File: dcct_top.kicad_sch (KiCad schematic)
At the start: 0 parts

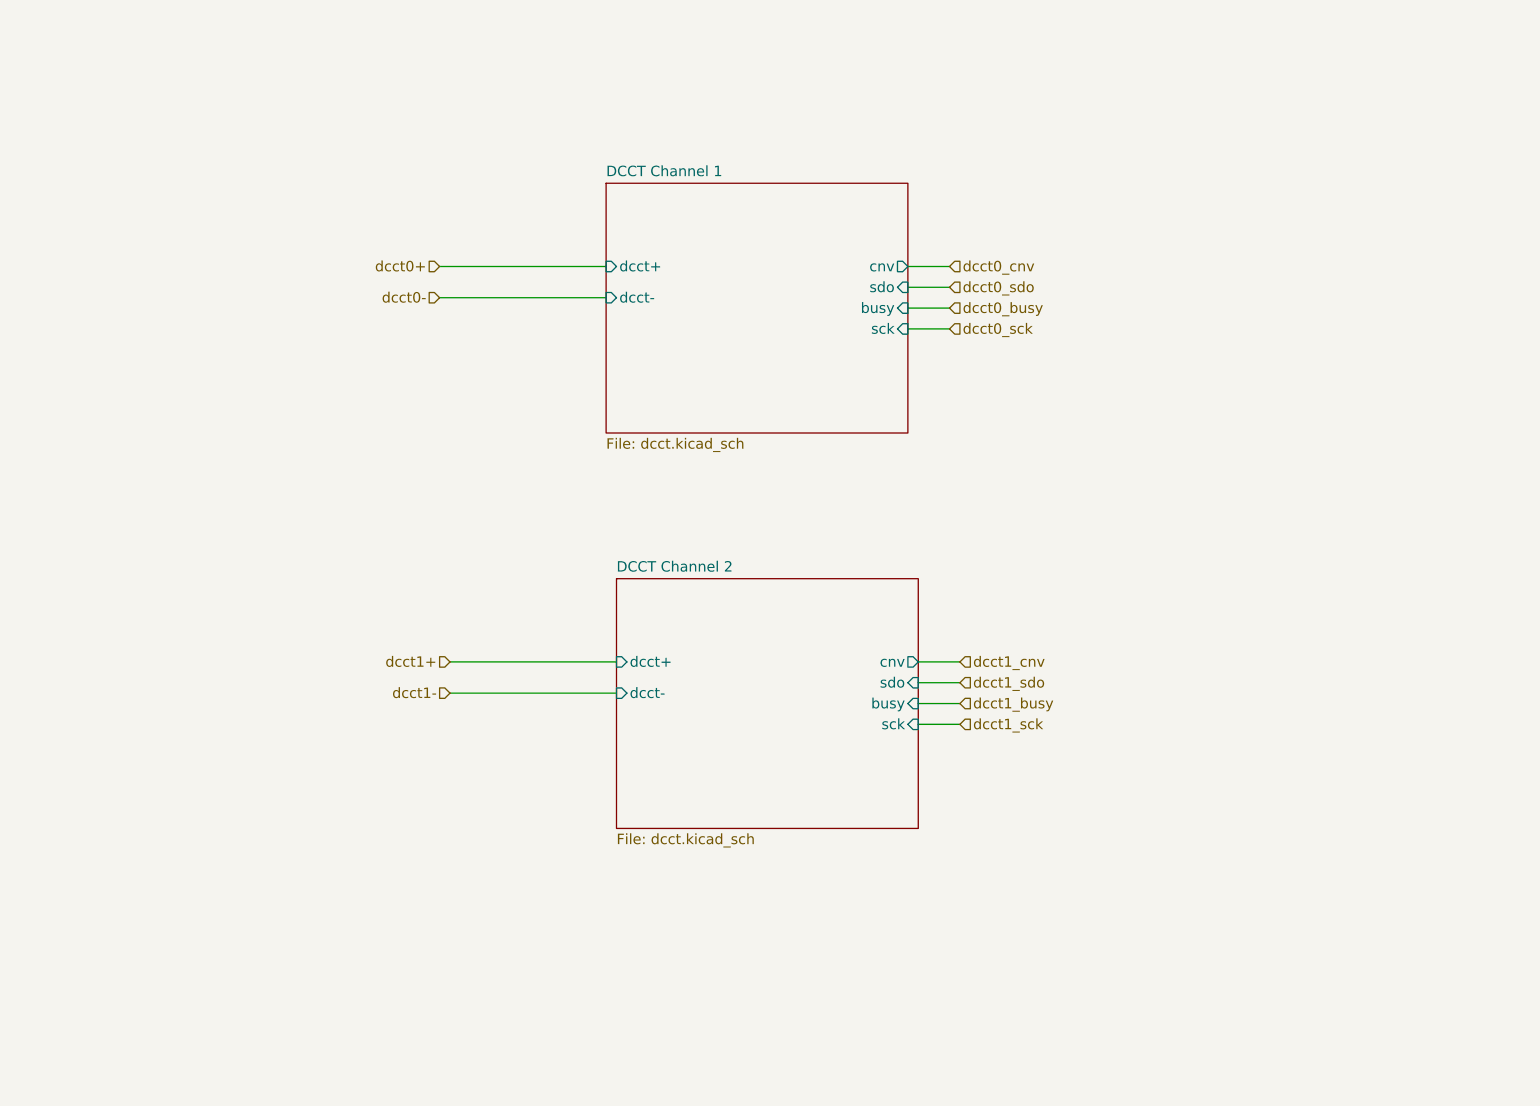
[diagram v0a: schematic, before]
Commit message: DAC and DCCT placement
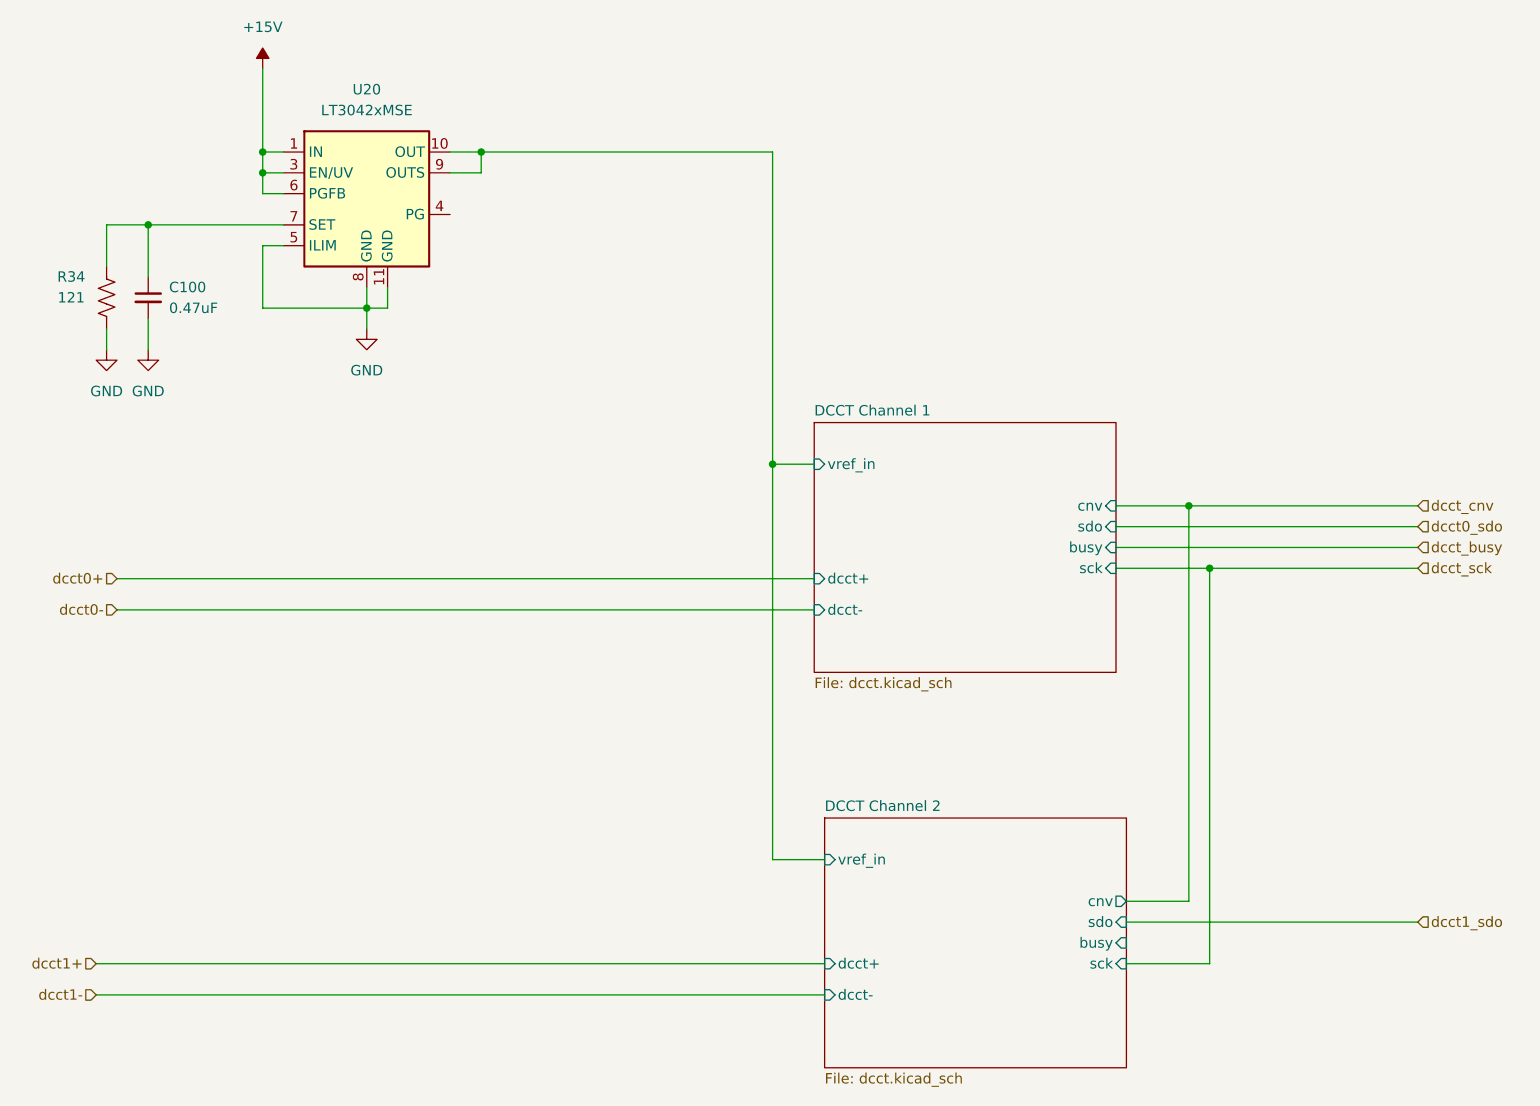
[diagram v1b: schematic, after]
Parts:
- added C100: 0.47uF, Capacitor_SMD:C_0402_1005Metric, symbol Device:C_Small
- added R34: 121, Resistor_SMD:R_0402_1005Metric, symbol Device:R_US
- added U20: LT3042xMSE, Package_SO:MSOP-10-1EP_3x3mm_P0.5mm_EP1.68x1.88mm, symbol PSC:LT3042xMSE
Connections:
- new net: C100.1, R34.2, U20.7 (SET)
- new net +15V: U20.1 (IN), U20.2 (IN), U20.3 (EN/UV), U20.6 (PGFB)
- new net DCCT Channel 1/vref_in: U20.10 (OUT), U20.9 (OUTS)
- new net GND: C100.2, R34.1, U20.11 (GND), U20.5 (ILIM), U20.8 (GND)
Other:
- sheet DCCT Channel 1 ports: added vref_in; removed none
- sheet DCCT Channel 2 ports: added vref_in; removed none

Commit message: finish rough placement
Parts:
- added C147, C153, C155, C157, C160, C166: 10uF, Capacitor_SMD:C_0603_1608Metric, symbol Device:C_Small
- added C148, C164, C170: 0.1uF, Capacitor_SMD:C_0402_1005Metric, symbol Device:C_Small
- added R57: 0, Resistor_SMD:R_0402_1005Metric, symbol Device:R_US
- added R59, R60: 10K, Resistor_SMD:R_0402_1005Metric, symbol Device:R_US
- added R61: 10, Resistor_SMD:R_0402_1005Metric, symbol Device:R_US
- added U32: LTC6655BHLS8-5, myparts:LTC6655, symbol PSC:LTC6655BHLS8-5
- added U35: LT6202CS5, myparts:LT6202CS5, symbol PSC:LT6202CS5
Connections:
- net GND: now also C147.2, C148.2, C153.2, C155.2, C157.2, C160.2, C164.2, C166.2, C170.2, R60.2, U32.3 (GND), U32.4 (GND), U32.5 (GND), U32.8 (GND), U35.2 (V-)
- net DCCT Channel 1/vref_in: no longer names the net of U20.10 (OUT), U20.9 (OUTS)
- net DCCT Channel 1/vref_in: now also C147.1, C148.1, U32.1 (IN), U32.2 (~SHDN)
- new net: C160.1, R59.1, R60.1, U35.3 (+)
- new net: C153.1, R57.2, U32.6 (VOUT_S), U32.7 (VOUT_F)
- new net: R61.2, U35.1, U35.4 (-)
- new net +5.3VA: C164.1, U35.5 (V+)
- new net DCCT Channel 1/adc_vref: C155.1, C157.1, R57.1, R59.2
- new net DCCT Channel 1/drv_vref: C166.1, C170.1, R61.1
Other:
- sheet DCCT Channel 1 ports: added adc_vref, drv_vref; removed vref_in
- sheet DCCT Channel 2 ports: added adc_vref, drv_vref; removed vref_in
- moved on the sheet: C100, R34, U20

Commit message: Finish layout
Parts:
- added C106: 10uF, Capacitor_SMD:C_0603_1608Metric, symbol Device:C_Small
- added C108: 0.1uF, Capacitor_SMD:C_0402_1005Metric, symbol Device:C_Small
- C100: value 0.47uF -> 10uF; footprint Capacitor_SMD:C_0402_1005Metric -> Capacitor_SMD:C_0603_1608Metric; MFG (none) -> Samsung; MFG_PN (none) -> CL10A106MA8NRNC; Voltage (none) -> 25V
- C147, C153, C155, C157, C160, C166: MFG (none) -> Samsung; MFG_PN (none) -> CL10A106MA8NRNC
- C148, C164, C170: MFG (none) -> Taiyo Yuden; MFG_PN (none) -> TMK105BJ104KV-F
- R34: value 121 -> 121K; MFG (none) -> Panasonic; MFG_PN (none) -> ERJ-2RKF1213X
- R57: MFG (none) -> Panasonic; MFG_PN (none) -> ERJ-2GE0R00X
- R59, R60: Cost (none) -> .01; MFG (none) -> Panasonic; MFG_PN (none) -> ERJ-2RKF1002X
- R61: Cost (none) -> .01; MFG (none) -> Panasonic; MFG_PN (none) -> ERJ-2RKF10R0X
- U20: Cost (none) -> 4.96; MFG (none) -> Analog Devices; MFG_PN (none) -> LT3042EMSE#TRPBF
- U32: Cost (none) -> 14.02; MFG (none) -> Analog Devices; MFG_PN (none) -> LTC6655BHLS8-5#PBF
- U35: Cost (none) -> 3.79; MFG (none) -> Analog Devices; MFG_PN (none) -> LT6202CS5#TRPBF
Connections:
- net +15V: now also C106.1, C108.1
- net GND: now also C106.2, C108.2
